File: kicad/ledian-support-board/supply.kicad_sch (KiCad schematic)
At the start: 7 parts, among them J6 Conn_01x02

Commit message: kicad: ledian-support-board: added titles to all pages
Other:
- title: (none) -> Power supply
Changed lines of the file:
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@@
 (kicad_sch (version 20230121) (generator eeschema)
   (paper "A4")
+  (title_block
+    (title "Power supply")
+  )
   (junction (at 119.38 60.96) (diameter 0) (color 0 0 0 0)
   )

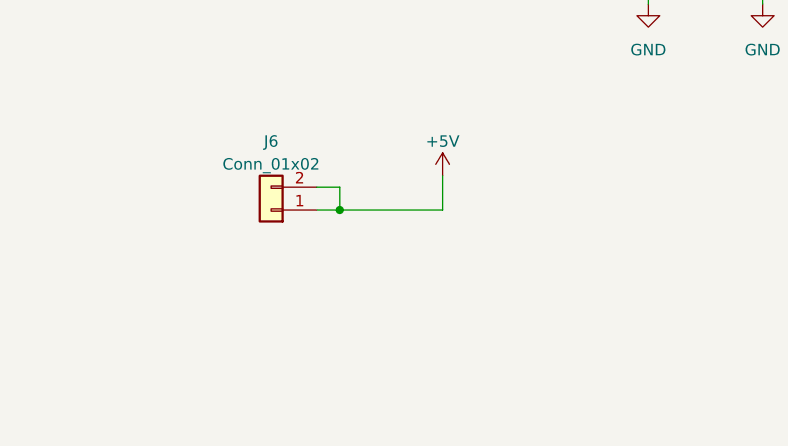
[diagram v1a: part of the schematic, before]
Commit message: kicad: ledian-support-board: added some comments to parts of the circuit
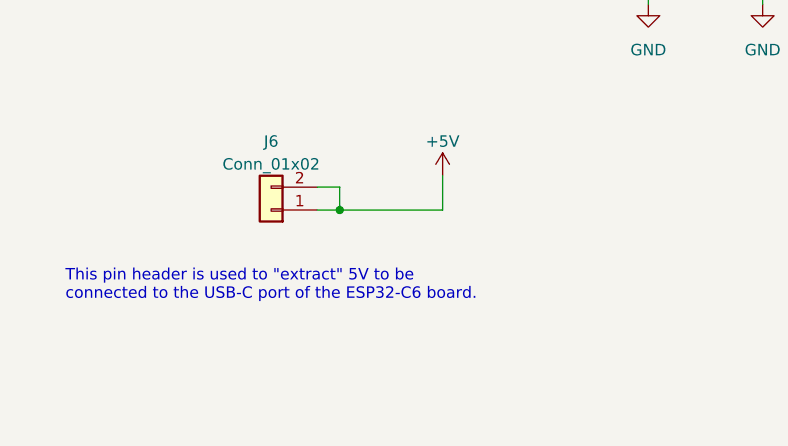
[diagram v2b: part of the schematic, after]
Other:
- note added: "This pin header is used to "extract" 5V to be connected to the USB-C port of the ESP32-C6 board."
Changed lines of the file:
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@@
     (stroke (width 0) (type default))
+  )
+  (text "This pin header is used to \"extract\" 5V to be\nconnected to the USB-C port of the ESP32-C6 board."
+    (at 54.61 109.22 0)
+    (effects (font (size 1.27 1.27)) (justify left bottom))
   )
   (symbol (lib_id "Device:C_Polarized") (at 172.72 68.58 0) (mirror y) (unit 1)
